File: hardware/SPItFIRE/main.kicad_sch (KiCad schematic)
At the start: 45 parts, among them J1 Compact Host, J10 ISP, J11 Joystick A, J12 Joystick B, J13 Peripheral DE-9, J14 Peripheral User Port, J2 User Port Host, J3 User Port Passthrough, J4 SD Card Adapter, J5 DeadOnRTC, J6 SPI_4, J7 SPI_5, J8 SPI_6, J9 SPI_7, U1 74HC138, U2 ATmega1284P-A, Y1 Crystal

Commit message: Crystal load capacitors C2 and C6 are 0201 instead of 0603 and were missing their 27 pF values in the schematic
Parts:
- C2, C6: footprint Capacitor_SMD:C_0201_0603Metric_Pad0.64x0.40mm_HandSolder -> Capacitor_SMD:C_0603_1608Metric_Pad1.08x0.95mm_HandSolder
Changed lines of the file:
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@@
 			)
 		)
-		(property "Footprint" "Capacitor_SMD:C_0201_0603Metric_Pad0.64x0.40mm_HandSolder"
+		(property "Footprint" "Capacitor_SMD:C_0603_1608Metric_Pad1.08x0.95mm_HandSolder"
 			(at 172.72 171.45 0)
 			(hide yes)
@@
 			)
 		)
-		(property "Footprint" "Capacitor_SMD:C_0201_0603Metric_Pad0.64x0.40mm_HandSolder"
+		(property "Footprint" "Capacitor_SMD:C_0603_1608Metric_Pad1.08x0.95mm_HandSolder"
 			(at 187.96 171.45 0)
 			(hide yes)

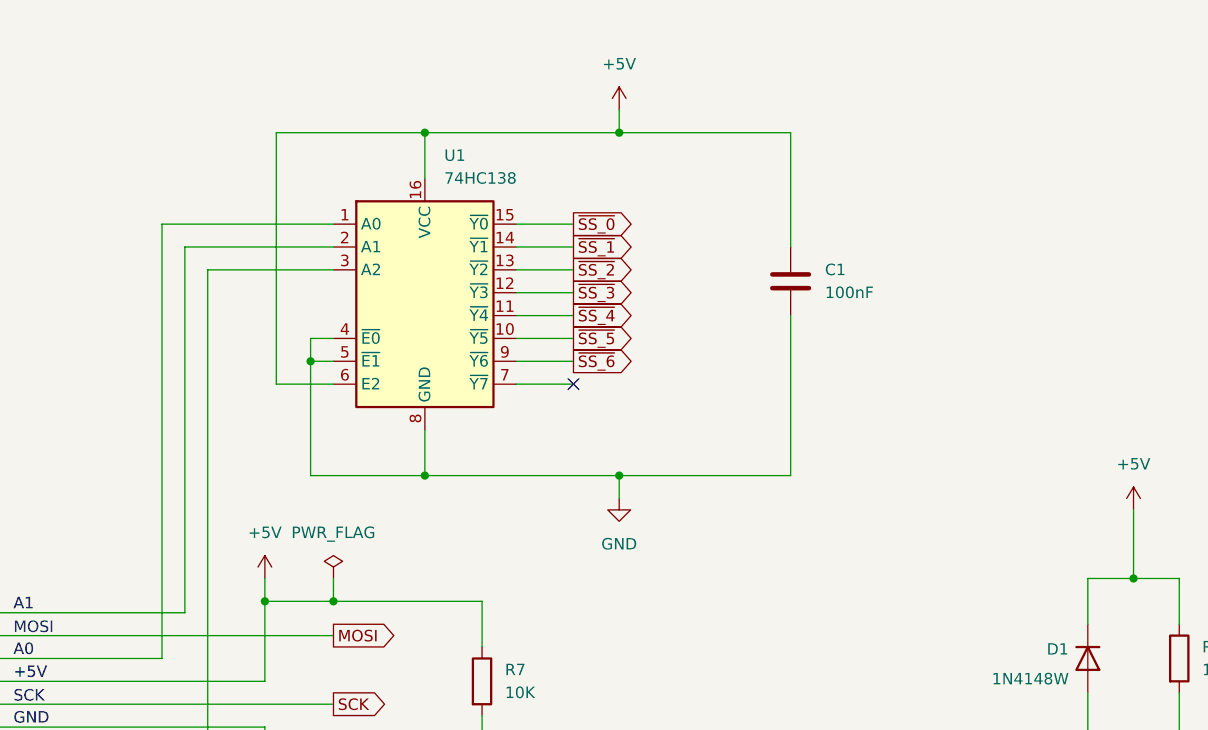
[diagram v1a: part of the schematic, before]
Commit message: Adds weak pull-ups to the address lines to give them definite state when the Compact is not connected
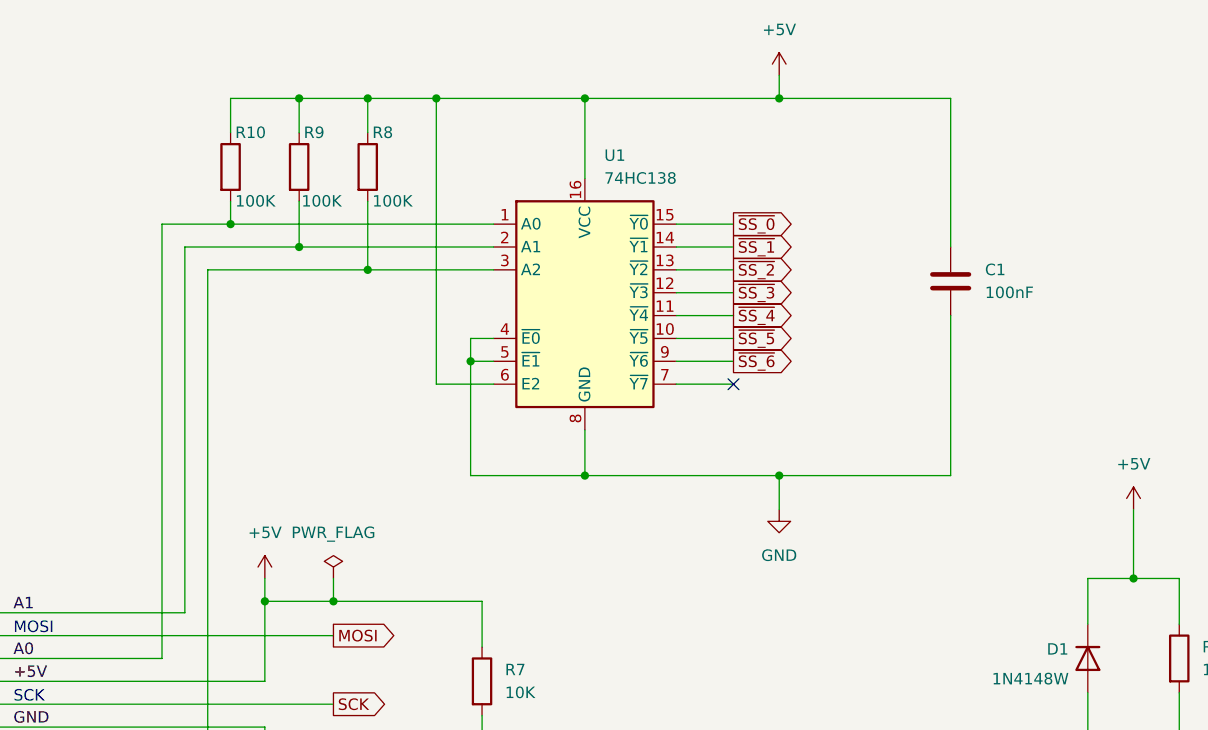
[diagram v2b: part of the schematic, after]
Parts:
- added R10, R8, R9: 100K, Resistor_SMD:R_0603_1608Metric_Pad0.98x0.95mm_HandSolder, symbol Device:R
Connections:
- net +5V: now also R10.1, R8.1, R9.1
- net A0: now also R10.2
- net A1: now also R9.2
- net A2: now also R8.2
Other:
- moved on the sheet: C1, U1

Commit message: Fixed the footprint of C3
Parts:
- C3: footprint LED_SMD:LED_0603_1608Metric_Pad1.05x0.95mm_HandSolder -> Capacitor_SMD:C_0603_1608Metric_Pad1.08x0.95mm_HandSolder
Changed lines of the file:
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@@
 			)
 		)
-		(property "Footprint" "LED_SMD:LED_0603_1608Metric_Pad1.05x0.95mm_HandSolder"
+		(property "Footprint" "Capacitor_SMD:C_0603_1608Metric_Pad1.08x0.95mm_HandSolder"
 			(at 174.9552 256.54 0)
 			(hide yes)
